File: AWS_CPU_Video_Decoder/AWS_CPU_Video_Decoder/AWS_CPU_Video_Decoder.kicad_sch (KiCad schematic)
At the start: 41 parts, among them J1 Conn_02x20_Odd_Even, J10 Conn_01x04_Pin, J11 Conn_01x04_Pin, J12 Conn_01x04_Pin, J13 Conn_01x04_Pin, J14 Conn_01x04_Pin, J15 Conn_01x04_Pin, J2 Conn_01x04_Pin, J3 Video, J4 Conn_01x04_Pin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

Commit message: Start of video board
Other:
- note added: "Note: use 19,20,21 for video"
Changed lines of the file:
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@@
+		)
+	)
+	(text "Note: use 19,20,21 for video"
+		(exclude_from_sim no)
+		(at 399.034 72.39 0)
+		(effects
+			(font
+				(size 1.27 1.27)
+			)
 		)
 	)

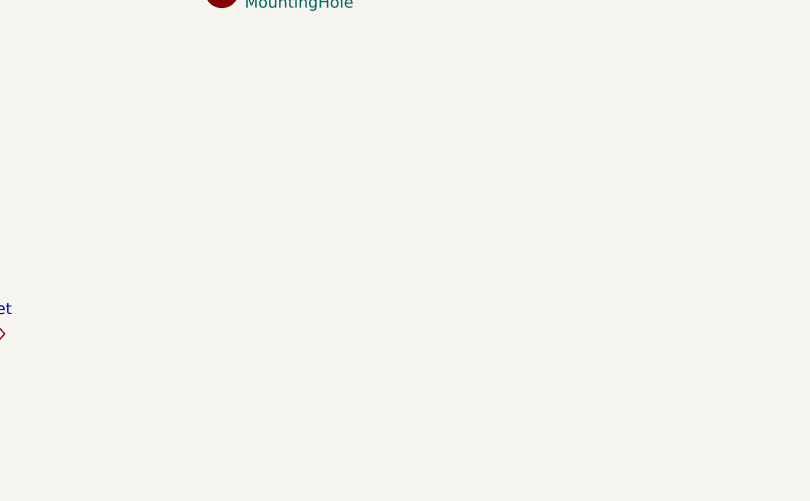
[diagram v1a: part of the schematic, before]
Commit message: Update PCB to fix floppy drive & update video software to capure all the screen
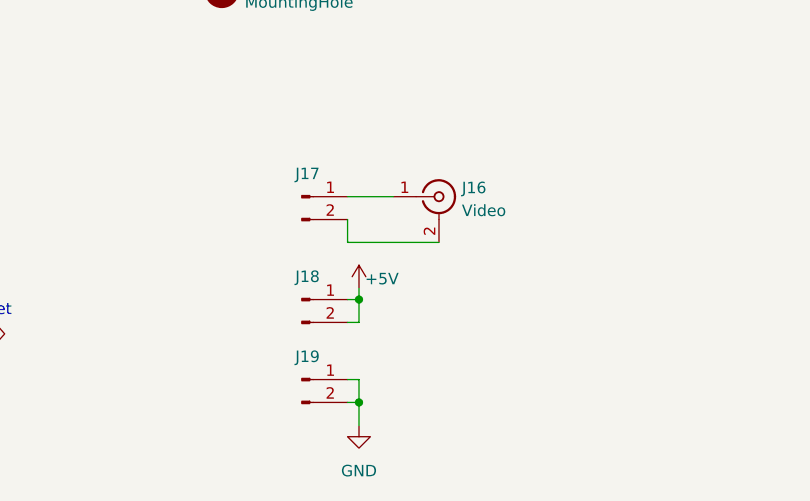
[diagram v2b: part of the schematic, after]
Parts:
- added J16: Video, local:SWITCHCRAFT_PJRAN1X1U04X, symbol Connector:Conn_Coaxial
- added J17, J18, J19: Conn_01x02_Pin, Connector_PinHeader_2.54mm:PinHeader_1x02_P2.54mm_Vertical, symbol Connector:Conn_01x02_Pin
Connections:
- net +5V: now also J18.1 (Pin_1), J18.2 (Pin_2)
- net GND: now also J19.1 (Pin_1), J19.2 (Pin_2)
- new net: J16.1 (In), J17.1 (Pin_1)
- new net: J16.2 (Ext), J17.2 (Pin_2)

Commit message: Added basic video
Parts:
- removed J17: Conn_01x02_Pin, Connector_PinHeader_2.54mm:PinHeader_1x02_P2.54mm_Vertical, symbol Connector:Conn_01x02_Pin
- added JP19, JP20, JP21: Jumper_2_Small_Bridged, Jumper:SolderJumper-2_P1.3mm_Bridged_RoundedPad1.0x1.5mm, symbol Jumper:Jumper_2_Small_Bridged
- added R1, R2, R3: 22R, Resistor_THT:R_Axial_DIN0204_L3.6mm_D1.6mm_P7.62mm_Horizontal, symbol Device:R
- added R10, R4, R5, R6: 330R, Resistor_THT:R_Axial_DIN0204_L3.6mm_D1.6mm_P7.62mm_Horizontal, symbol Device:R
- added R7, R8, R9: 100R, Resistor_THT:R_Axial_DIN0204_L3.6mm_D1.6mm_P7.62mm_Horizontal, symbol Device:R
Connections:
- net GND: now also J16.2 (Ext), R10.2
- net at J16.1 (In): now also R6.1, R8.1
- net GPIO20 renamed DAC0
- net DAC0: now also JP21.2 (B)
- net GPIO21 renamed DAC1
- net DAC1: now also JP20.2 (B)
- net GPIO22 renamed DAC2
- net DAC2: now also JP19.2 (B)
- new net: R4.1, R7.1, R9.2
- new net: R10.1, R7.2
- new net: R2.1, R5.2
- new net: JP20.1 (A), R2.2
- new net: R3.1, R6.2
- new net: JP19.1 (A), R3.2
- new net: R1.1, R4.2
- new net: JP21.1 (A), R1.2
- new net: R5.1, R8.2, R9.1
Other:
- moved on the sheet: H1, J16, J18, J19, SW1

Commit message: Fix level shifters
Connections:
- net AF: now also U4.11 (HV2); no longer U4.5 (LV3)
- net AF_LV: now also U4.2 (LV2); no longer U4.8 (HV3)
- net CC0: now also U2.8 (HV3); no longer U2.2 (LV2)
- net CC0_LV: now also U2.5 (LV3); no longer U2.11 (HV2)
- net CC1: now also U1.8 (HV3); no longer U1.2 (LV2)
- net CC1_LV: now also U1.5 (LV3); no longer U1.11 (HV2)
- net CC2: now also U2.7 (HV4); no longer U2.1 (LV1)
- net CC2_LV: now also U2.6 (LV4); no longer U2.12 (HV1)
- net CC3: now also U1.7 (HV4); no longer U1.1 (LV1)
- net CC3_LV: now also U1.6 (LV4); no longer U1.12 (HV1)
- net CC4: now also U3.12 (HV1); no longer U3.6 (LV4)
- net CC4_LV: now also U3.1 (LV1); no longer U3.7 (HV4)
- net CC5: now also U2.12 (HV1); no longer U2.6 (LV4)
- net CC5_LV: now also U2.1 (LV1); no longer U2.7 (HV4)
- net CC6: now also U3.11 (HV2); no longer U3.5 (LV3)
- net CC6_LV: now also U3.2 (LV2); no longer U3.8 (HV3)
- net CCLK: now also U1.11 (HV2); no longer U1.5 (LV3)
- net CCLK_LV: now also U1.2 (LV2); no longer U1.8 (HV3)
- net CPIX: now also U1.12 (HV1); no longer U1.6 (LV4)
- net CPIX_LV: now also U1.1 (LV1); no longer U1.7 (HV4)
- net DVSP: now also U5.12 (HV1); no longer U5.6 (LV4)
- net DVSP_LV: now also U5.1 (LV1); no longer U5.7 (HV4)
- net HB: now also U4.12 (HV1); no longer U4.6 (LV4)
- net HBS: now also U3.8 (HV3); no longer U3.2 (LV2)
- net HBS_LV: now also U3.5 (LV3); no longer U3.11 (HV2)
- net HB_LV: now also U4.1 (LV1); no longer U4.7 (HV4)
- net HSYNC: now also U4.8 (HV3); no longer U4.2 (LV2)
- net HSYNC_LV: now also U4.5 (LV3); no longer U4.11 (HV2)
- net RV: now also U2.11 (HV2); no longer U2.5 (LV3)
- net RV_LV: now also U2.2 (LV2); no longer U2.8 (HV3)
- net UL: now also U3.7 (HV4); no longer U3.1 (LV1)
- net UL_LV: now also U3.6 (LV4); no longer U3.12 (HV1)
- net VSYNC: now also U4.7 (HV4); no longer U4.1 (LV1)
- net VSYNC_LV: now also U4.6 (LV4); no longer U4.12 (HV1)
- net ~{RESET_LV}: now also U5.2 (LV2); no longer U5.8 (HV3)
- net ~{RESET}: now also U5.11 (HV2); no longer U5.5 (LV3)
- net at J11.1 (Pin_1): now also U6.7 (HV4); no longer U6.1 (LV1)
- net at J11.2 (Pin_2): now also U6.8 (HV3); no longer U6.2 (LV2)
- net at J11.3 (Pin_3): now also U6.11 (HV2); no longer U6.5 (LV3)
- net at J11.4 (Pin_4): now also U6.12 (HV1); no longer U6.6 (LV4)
- net at J8.1 (Pin_1): now also U5.6 (LV4); no longer U5.12 (HV1)
- net at J8.2 (Pin_2): now also U5.5 (LV3); no longer U5.11 (HV2)
- net at J9.2 (Pin_2): now also U6.5 (LV3); no longer U6.11 (HV2)
- net at J9.1 (Pin_1): now also U6.6 (LV4); no longer U6.12 (HV1)
- net at J9.4 (Pin_4): now also U6.1 (LV1); no longer U6.7 (HV4)
- net at J9.3 (Pin_3): now also U6.2 (LV2); no longer U6.8 (HV3)
- net at J13.1 (Pin_1): now also U5.7 (HV4); no longer U5.1 (LV1)
- net at J13.2 (Pin_2): now also U5.8 (HV3); no longer U5.2 (LV2)
- no-connect marks 28 -> 30
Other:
- note added: "Attribute Select - Underline - Video Suppress - Reverse Video"
- note added: "Font Select"
- note added: "RESET VSYNC HSYNC CCLK CC0-CC6 (7) AF - Alternate Font UL - Underline (This blanks all but row 9, can't underline fonts) VS - Video Suppress (Does blinking) RV - Reverse Video (This wokrs with blinking and underline) HB - Half-Bright"
- note removed: "RESET VSYNC HSYNC CCLK CC0-CC6 (7) AF - Alternate Font UL - Underline (This blanks all but row 9) VS - Video Suppress (Does blinking) RV - Reverse Video (This wokrs with blinking and underline) HB - Half-Bright"
- moved on the sheet: J10, J11, J12, J13, J14, J15, J2, J4, J6, J7, J8, J9

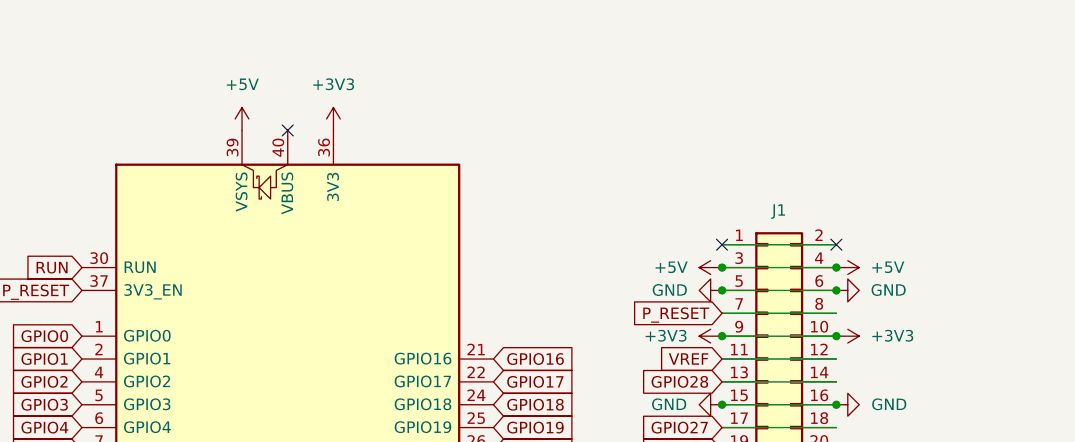
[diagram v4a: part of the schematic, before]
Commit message: Added Schottky Diode
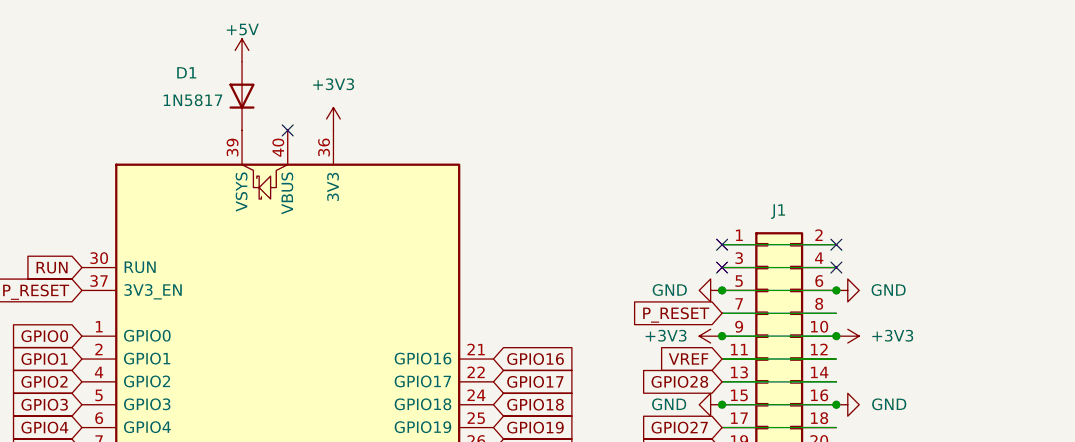
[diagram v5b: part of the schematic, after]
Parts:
- added D1: 1N5817, Diode_THT:D_5W_P12.70mm_Horizontal, symbol Device:D
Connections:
- net +5V: now also D1.2 (A); no longer A2.39 (VSYS), J1.3 (Pin_3), J1.4 (Pin_4)
- new net: A2.39 (VSYS), D1.1 (K)
- new net: J1.3 (Pin_3), J1.4 (Pin_4)
- no-connect marks 30 -> 32
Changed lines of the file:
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@@
 	)
 	(junction
-		(at 370.84 39.37)
-		(diameter 0)
-		(color 0 0 0 0)
-	)
-	(junction
 		(at 257.81 54.61)
 		(diameter 0)
@@
 	)
 	(junction
-		(at 383.54 39.37)
-		(diameter 0)
-		(color 0 0 0 0)
-	)
-	(junction
 		(at 369.57 224.79)
 		(diameter 0)
@@
 	)
 	(no_connect
+		(at 383.54 39.37)
+	)
+	(no_connect
 		(at 120.65 109.22)
 	)
@@
 	)
 	(no_connect
+		(at 370.84 39.37)
+	)
+	(no_connect
 		(at 257.81 39.37)
 	)
@@
 	)
 	(symbol
-		(lib_id "power:+5V")
-		(at 383.54 39.37 270)
-		(unit 1)
-		(exclude_from_sim no)
-		(in_bom yes)
-		(on_board yes)
-		(dnp no)
-		(fields_autoplaced yes)
-		(property "Reference" "#PWR051"
-			(at 379.73 39.37 0)
-			(effects
-				(font
-					(size 1.27 1.27)
-				)
-				(hide yes)
-			)
-		)
-		(property "Value" "+5V"
-			(at 387.35 39.3699 90)
-			(effects
-				(font
-					(size 1.27 1.27)
-				)
-				(justify left)
-			)
-		)
-		(property "Footprint" ""
-			(at 383.54 39.37 0)
-			(effects
-				(font
-					(size 1.27 1.27)
-				)
-				(hide yes)
-			)
-		)
-		(property "Datasheet" ""
-			(at 383.54 39.37 0)
-			(effects
-				(font
-					(size 1.27 1.27)
-				)
-				(hide yes)
-			)
-		)
-		(property "Description" "Power symbol creates a global label with name \"+5V\""
-			(at 383.54 39.37 0)
-			(effects
-				(font
-					(size 1.27 1.27)
-				)
-				(hide yes)
-			)
-		)
-		(pin "1"
-		)
-		(instances
-			(project "AWS_CPU_Video_Decoder"
-				(path "/fd80293a-a4d3-4f78-b100-347c7998a86f"
-					(reference "#PWR051")
-					(unit 1)
-				)
-			)
-		)
-	)
-	(symbol
 		(lib_id "Device:R")
 		(at 156.21 265.43 0)
@@
 	(symbol
 		(lib_id "power:+5V")
-		(at 317.5 24.13 0)
+		(at 317.5 16.51 0)
 		(unit 1)
 		(exclude_from_sim no)
@@
 		(on_board yes)
 		(dnp no)
-		(fields_autoplaced yes)
 		(property "Reference" "#PWR013"
-			(at 317.5 27.94 0)
+			(at 317.5 20.32 0)
 			(effects
 				(font
@@
 		)
 		(property "Value" "+5V"
-			(at 317.5 19.05 0)
+			(at 317.5 12.954 0)
 			(effects
 				(font
@@
 		)
 		(property "Footprint" ""
-			(at 317.5 24.13 0)
+			(at 317.5 16.51 0)
 			(effects
 				(font
@@
 		)
 		(property "Datasheet" ""
-			(at 317.5 24.13 0)
+			(at 317.5 16.51 0)
 			(effects
 				(font
@@
 		)
 		(property "Description" "Power symbol creates a global label with name \"+5V\""
-			(at 317.5 24.13 0)
+			(at 317.5 16.51 0)
 			(effects
 				(font
@@
 	)
 	(symbol
+		(lib_id "Device:D")
+		(at 317.5 20.32 90)
+		(unit 1)
+		(exclude_from_sim no)
+		(in_bom yes)
+		(on_board yes)
+		(dnp no)
+		(property "Reference" "D1"
+			(at 310.134 17.78 90)
+			(effects
+				(font
+					(size 1.27 1.27)
+				)
+				(justify right)
+			)
+		)
+		(property "Value" "1N5817"
+			(at 308.61 20.828 90)
+			(effects
+				(font
+					(size 1.27 1.27)
+				)
+				(justify right)
+			)
+		)
+		(property "Footprint" "Diode_THT:D_5W_P12.70mm_Horizontal"
+			(at 317.5 20.32 0)
+			(effects
+				(font
+					(size 1.27 1.27)
+				)
+				(hide yes)
+			)
+		)
+		(property "Datasheet" "~"
+			(at 317.5 20.32 0)
+			(effects
+				(font
+					(size 1.27 1.27)
+				)
+				(hide yes)
+			)
+		)
+		(property "Description" "Diode"
+			(at 317.5 20.32 0)
+			(effects
+				(font
+					(size 1.27 1.27)
+				)
+				(hide yes)
+			)
+		)
+		(property "Sim.Device" "D"
+			(at 317.5 20.32 0)
+			(effects
+				(font
+					(size 1.27 1.27)
+				)
+				(hide yes)
+			)
+		)
+		(property "Sim.Pins" "1=K 2=A"
+			(at 317.5 20.32 0)
+			(effects
+				(font
+					(size 1.27 1.27)
+				)
+				(hide yes)
+			)
+		)
+		(pin "2"
+		)
+		(pin "1"
+		)
+		(instances
+			(project ""
+				(path "/fd80293a-a4d3-4f78-b100-347c7998a86f"
+					(reference "D1")
+					(unit 1)
+				)
+			)
+		)
+	)
+	(symbol
 		(lib_id "Device:R")
 		(at 162.56 250.19 90)
@@
 					(unit 1)
 				)
-			)
-		)
-	)
-	(symbol
-		(lib_id "power:+5V")
-		(at 370.84 39.37 90)
-		(unit 1)
-		(exclude_from_sim no)
-		(in_bom yes)
-		(on_board yes)
-		(dnp no)
-		(fields_autoplaced yes)
-		(property "Reference" "#PWR050"
-			(at 374.65 39.37 0)
-			(effects
-				(font
-					(size 1.27 1.27)
-				)
-				(hide yes)
-			)
-		)
-		(property "Value" "+5V"
-			(at 367.03 39.3699 90)
-			(effects
-				(font
-					(size 1.27 1.27)
-				)
-				(justify left)
-			)
-		)
-		(property "Footprint" ""
-			(at 370.84 39.37 0)
-			(effects
-				(font
-					(size 1.27 1.27)
-				)
-				(hide yes)
-			)
-		)
-		(property "Datasheet" ""
-			(at 370.84 39.37 0)
-			(effects
-				(font
-					(size 1.27 1.27)
-				)
-				(hide yes)
-			)
-		)
-		(property "Description" "Power symbol creates a global label with name \"+5V\""
-			(at 370.84 39.37 0)
-			(effects
-				(font
-					(size 1.27 1.27)
-				)
-				(hide yes)
-			)
-		)
-		(pin "1"
-		)
-		(instances
-			(project "AWS_CPU_Video_Decoder"
-				(path "/fd80293a-a4d3-4f78-b100-347c7998a86f"
-					(reference "#PWR050")
-					(unit 1)
-				)

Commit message: Fixed rendering issue
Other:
- note added: "Each font has four display modes. 256 * 4 = 1024 glyphs UL, Blank, RUL, RBlank, HUL, HRUL, HRBlank (+7)"
